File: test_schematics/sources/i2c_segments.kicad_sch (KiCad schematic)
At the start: 23 parts, among them Q1 BSS138, Q2 BSS138, Q3 BSS138, Q4 BSS138, U10 PCA9306, U11 PCA9536DP, U5 STM32F030F4Px, U6 PCA9536DP, U7 PCA9536DP, U8 PCA9536DP, U9 PCA9536DP

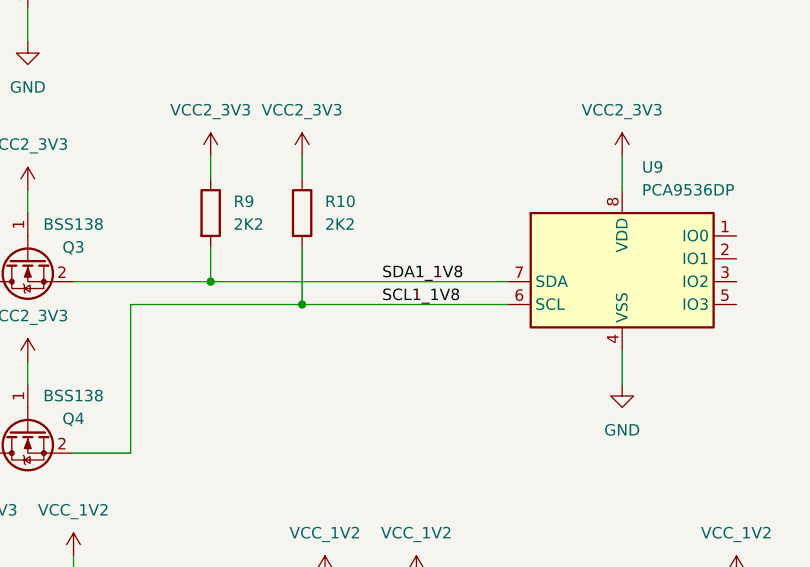
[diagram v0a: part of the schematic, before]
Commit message: feat: find I2C buses and their pull-ups.
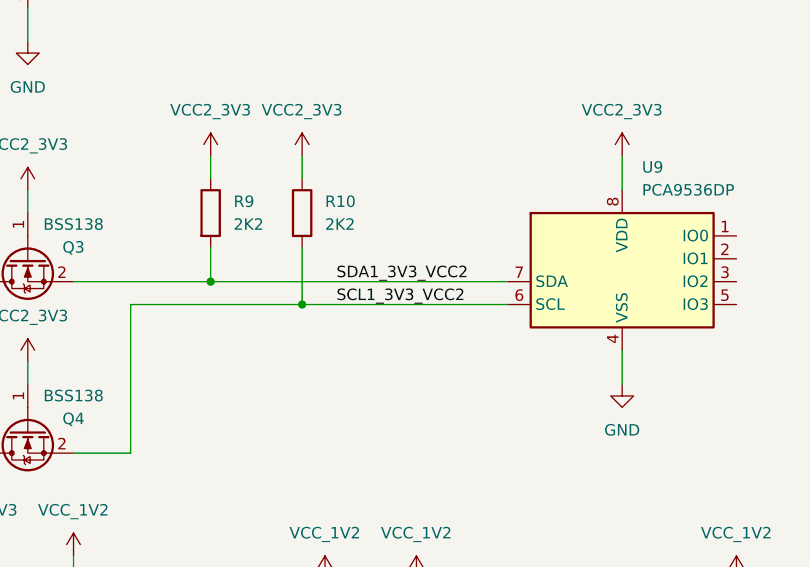
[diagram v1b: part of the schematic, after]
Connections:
- net SCL1_1V8: no longer Q4.2 (S), R10.2, U9.6 (SCL)
- net SDA1_1V8: no longer Q3.2 (S), R9.2, U9.7 (SDA)
- new net SCL1_3V3_VCC2: Q4.2 (S), R10.2, U9.6 (SCL)
- new net SDA1_3V3_VCC2: Q3.2 (S), R9.2, U9.7 (SDA)
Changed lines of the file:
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@@
+	(wire
+		(pts
+			(xy 210.82 172.72) (xy 233.68 172.72)
+		)
+		(stroke
+			(width 0)
+			(type default)
+		)
+	)
 	(wire
 		(pts
@@
 		(pts
 			(xy 139.7 170.18) (xy 139.7 132.08)
-		)
-		(stroke
-			(width 0)
-			(type default)
-		)
-	)
-	(wire
-		(pts
-			(xy 233.68 172.72) (xy 210.82 172.72)
 		)
 		(stroke
@@
 		)
 	)
-	(label "SCL1_1V8"
-		(at 219.71 172.72 0)
+	(label "SCL1_3V3_VCC2"
+		(at 214.63 172.72 0)
 		(fields_autoplaced yes)
 		(effects
@@
 		)
 	)
-	(label "SDA1_1V8"
-		(at 219.71 170.18 0)
-		(fields_autoplaced yes)
-		(effects
+	(label "SDA1_3V3_VCC2"
+		(at 214.63 170.18 0)
+		(fields_autoplaced yes)
+		(effects

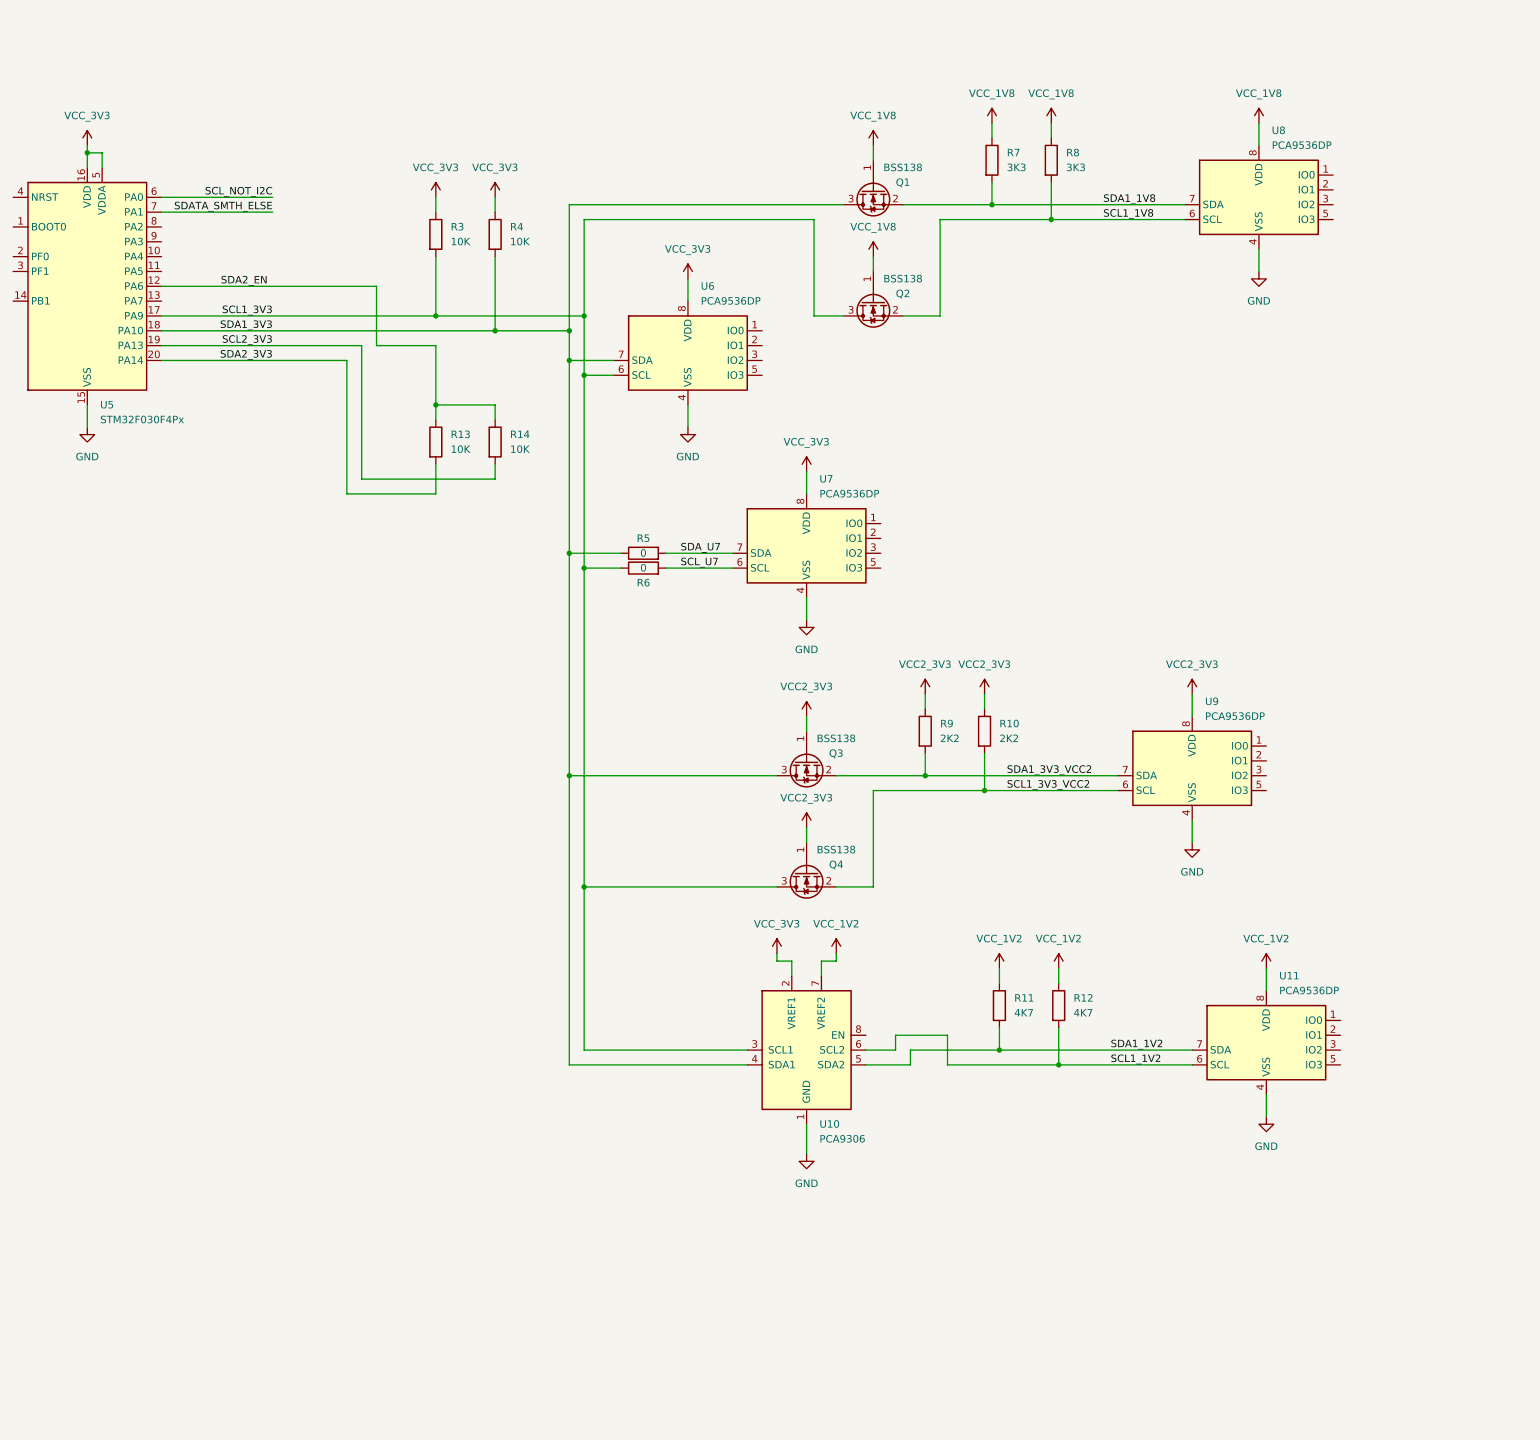
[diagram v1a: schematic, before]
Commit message: refactor: re-annotate test schematics with page X100 designators.
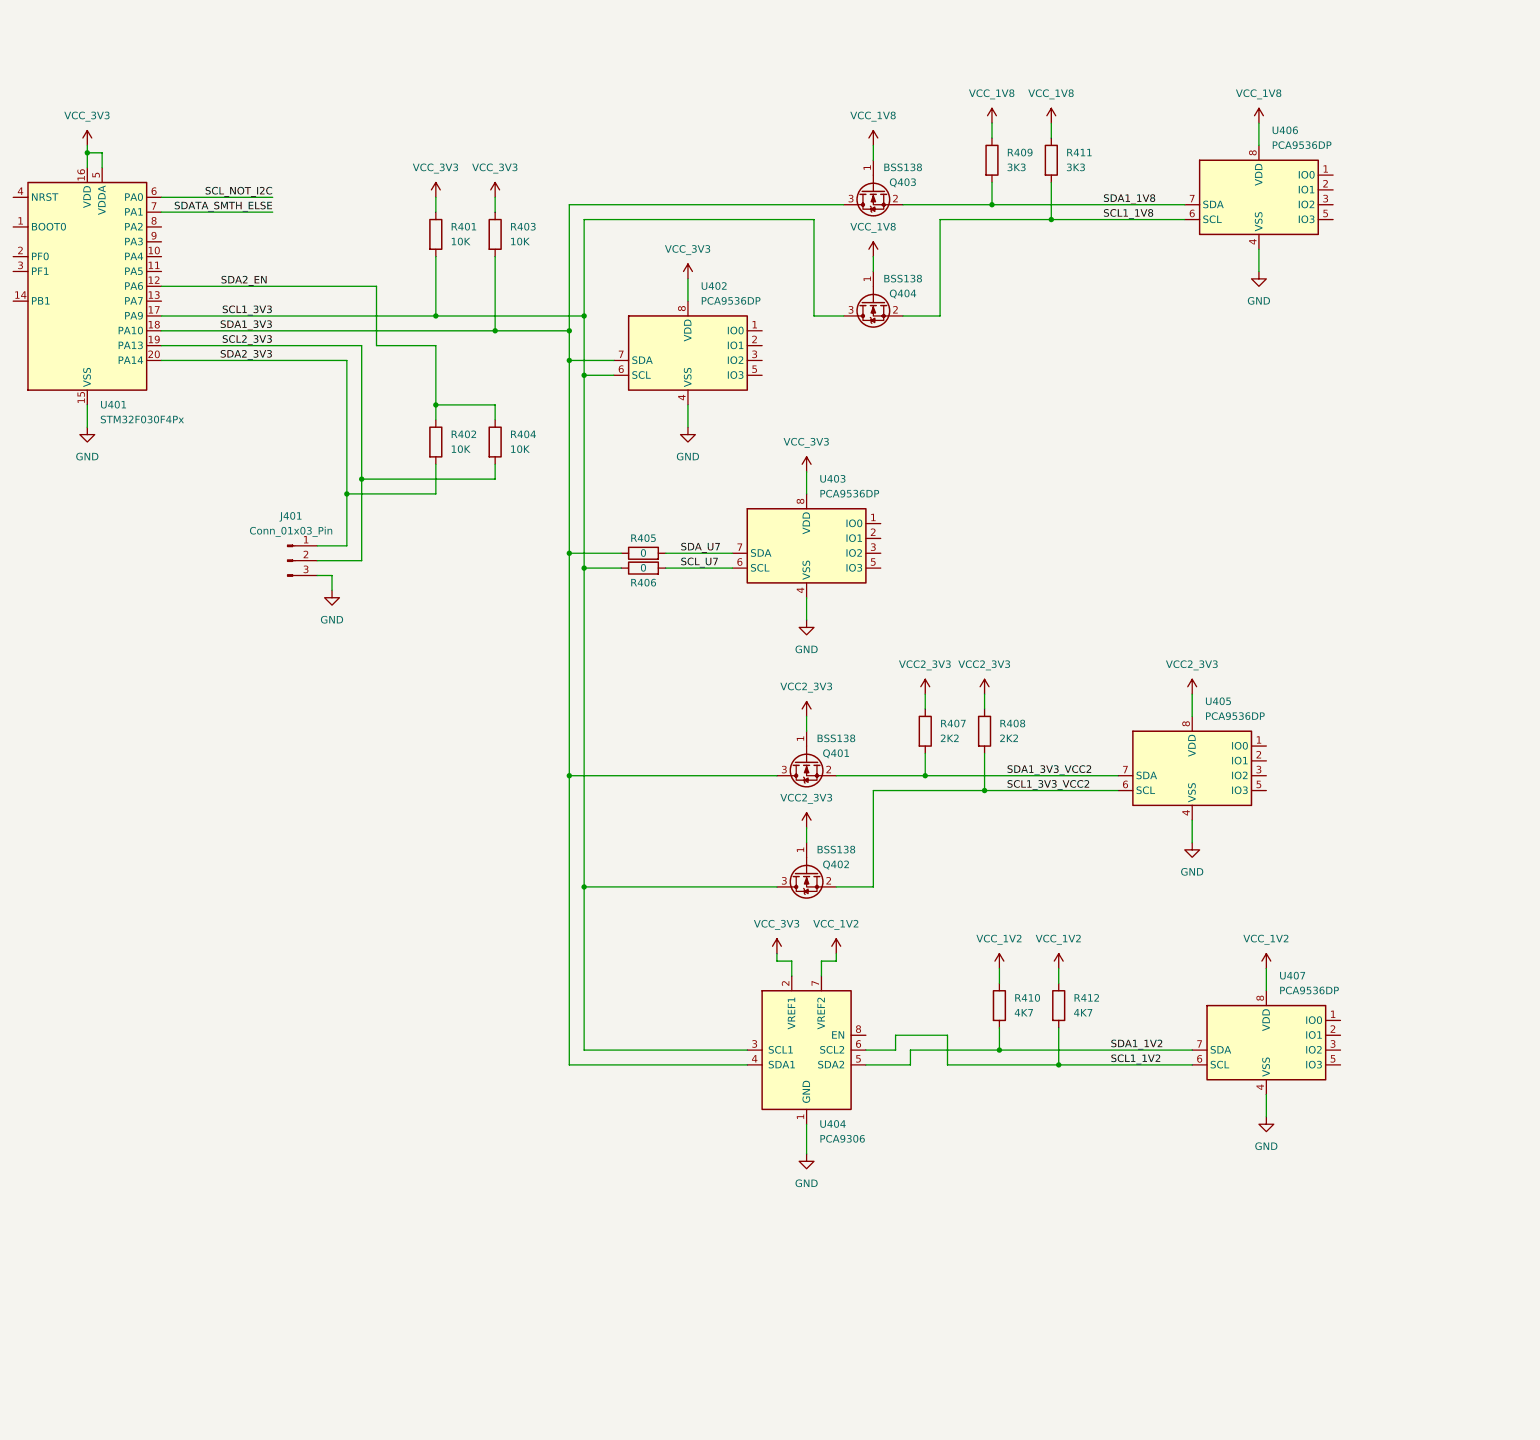
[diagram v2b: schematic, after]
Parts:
- added J401: Conn_01x03_Pin, symbol Connector:Conn_01x03_Pin
- renumbered Q3 to Q401, Q4 to Q402, Q1 to Q403, Q2 to Q404, R3 to R401, R13 to R402, R4 to R403, R14 to R404, R5 to R405, R6 to R406, R9 to R407, R10 to R408, R7 to R409, R11 to R410, R8 to R411, R12 to R412, U5 to U401, U6 to U402, U7 to U403, U10 to U404, U9 to U405, U8 to U406, U11 to U407
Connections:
- net GND: now also J401.3 (Pin_3)
- net SCL2_3V3: now also J401.2 (Pin_2)
- net SDA2_3V3: now also J401.1 (Pin_1)

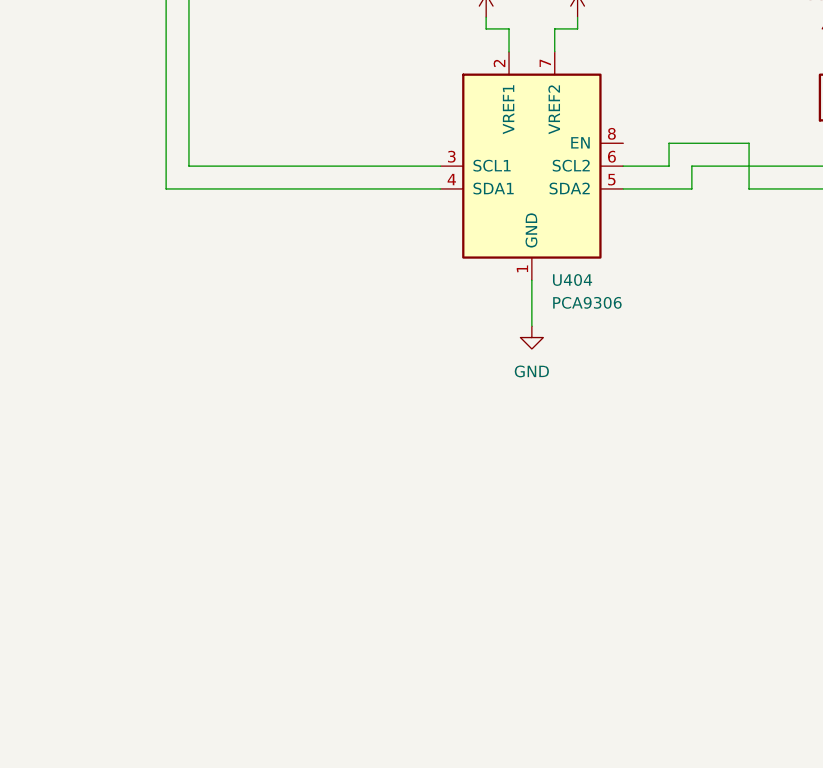
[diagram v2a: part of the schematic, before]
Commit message: feat: find redundant pull-ups.
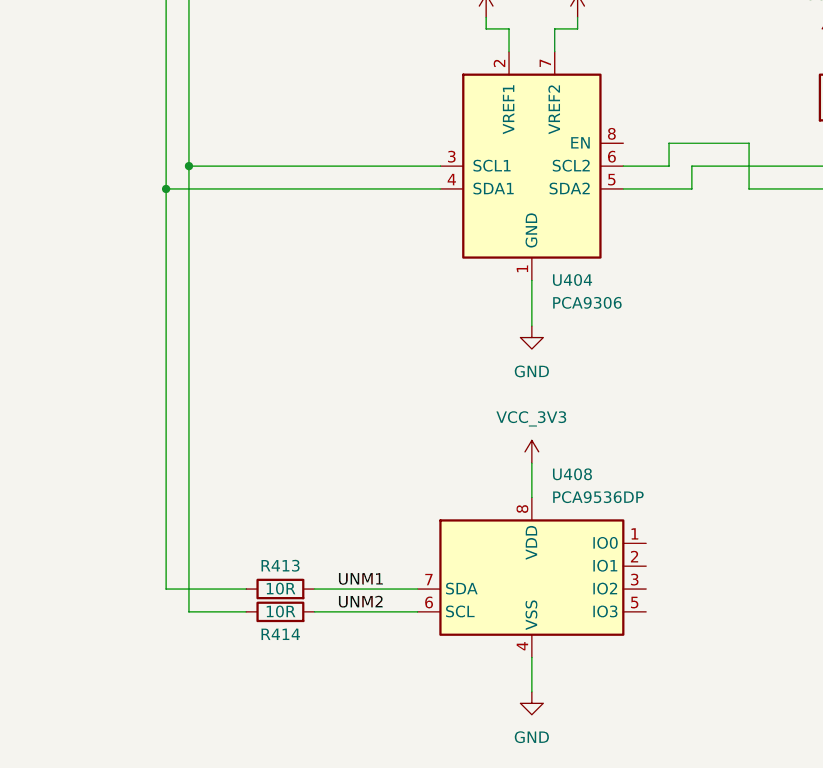
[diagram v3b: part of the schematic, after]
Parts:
- added R413, R414: 10R, symbol Device:R
- added U408: PCA9536DP, Package_SO:TSSOP-8_3x3mm_P0.65mm, symbol Interface_Expansion:PCA9536DP
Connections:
- net GND: now also U408.4 (VSS)
- net SCL1_3V3: now also R414.1
- net SDA1_3V3: now also R413.1
- net VCC_3V3: now also U408.8 (VDD)
- new net UNM1: R413.2, U408.7 (SDA)
- new net UNM2: R414.2, U408.6 (SCL)

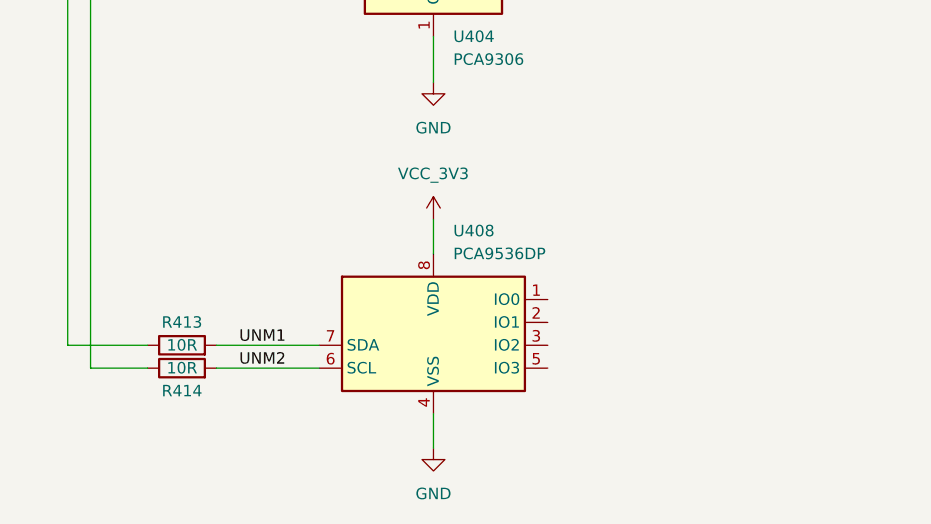
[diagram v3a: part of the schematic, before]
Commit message: feat: look for I2C buses interconnect.
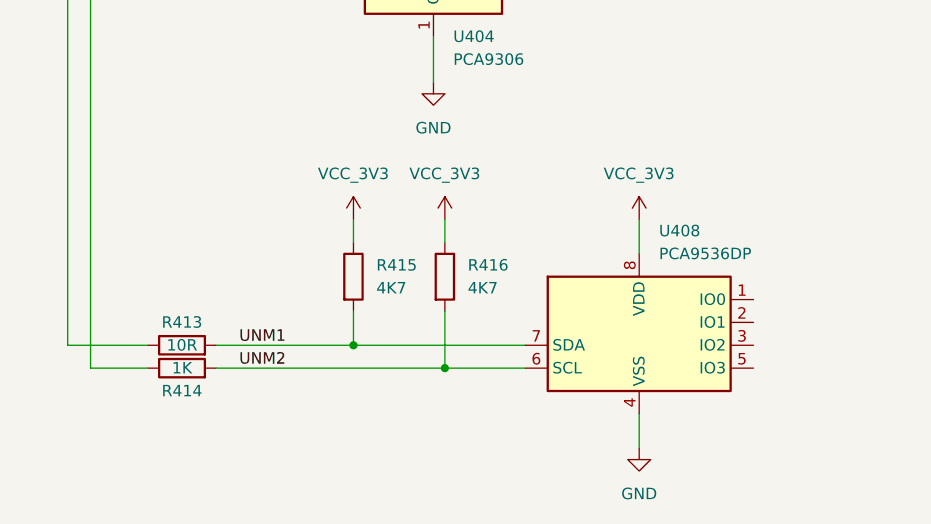
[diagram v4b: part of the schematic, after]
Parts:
- added R415, R416: 4K7, symbol Device:R
- R414: value 10R -> 1K
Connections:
- net UNM1: now also R415.2
- net UNM2: now also R416.2
- net VCC_3V3: now also R415.1, R416.1
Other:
- moved on the sheet: U408
